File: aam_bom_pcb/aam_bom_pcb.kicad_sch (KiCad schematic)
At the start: 42 parts, among them J1 USB_C_Receptacle_USB2.0_16P, U1 BQ25120AYFPR, U3 STM32WB5MMG, U4 TLV320DAC3203IRGER

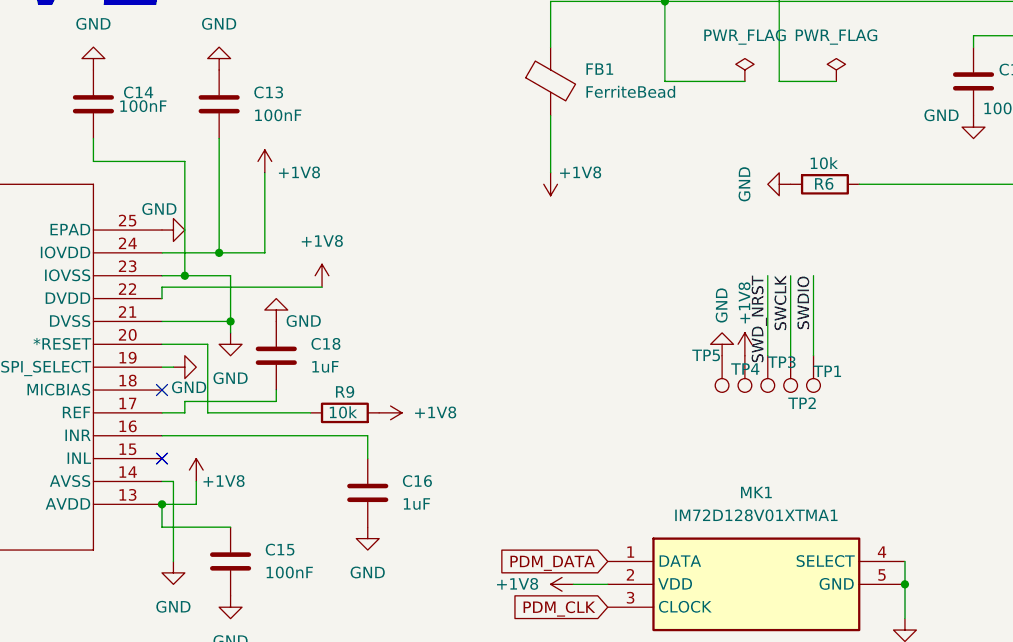
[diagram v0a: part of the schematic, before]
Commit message: Integrar footprint de programación Tag-Connect TC2030-NL y validar esquemático
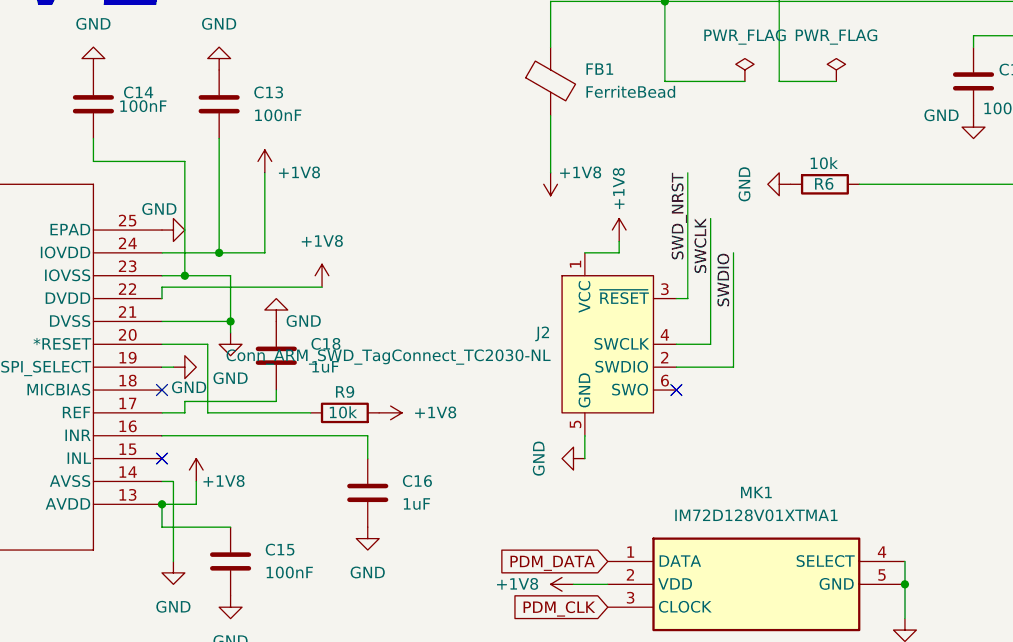
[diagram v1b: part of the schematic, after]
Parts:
- removed TP1, TP2, TP3, TP4, TP5: TestPoint, TestPoint:TestPoint_Pad_D1.5mm, symbol Connector:TestPoint
- added J2: Conn_ARM_SWD_TagConnect_TC2030-NL, Connector:Tag-Connect_TC2030-IDC-NL_2x03_P1.27mm_Vertical, symbol Connector:Conn_ARM_SWD_TagConnect_TC2030-NL
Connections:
- net +1V8: now also J2.1 (VCC)
- net GND: now also J2.5 (GND)
- net SWCLK: now also J2.4 (SWCLK)
- net SWDIO: now also J2.2 (SWDIO)
- net SWD_NRST: now also J2.3 (~{RESET})
- no-connect marks 78 -> 79
